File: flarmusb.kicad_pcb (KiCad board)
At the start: 2 copper layers, 22 parts, among them J1 USB_B_Micro, J2 Barrel_Jack_Switch, J3 RJ45_Shielded, U1 LM3940-3.3, U2 CH340G, U3 MAX3232, Y1 12M

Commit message: PCB traced
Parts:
- added REF**: OSHW-Logo2_9.8x8mm_SilkScreen, Symbol:OSHW-Logo2_9.8x8mm_SilkScreen, B.Cu at (110.7, 82.8)
- moved R1 36.6 mm to (128.5, 84.8), turned to 90 degrees
- moved C4 29.3 mm to (123.4, 78.2), turned to 180 degrees
- moved C7 27.6 mm to (126.5, 81.3), turned to 90 degrees
- moved C5 27.3 mm to (126.5, 84.8), turned to 90 degrees
- moved C9 26.9 mm to (135.1, 73.7), turned to 90 degrees
- moved D3 26.3 mm to (128.5, 77.7), turned to 270 degrees
- moved C6 25.5 mm to (119.9, 78.2), turned to 180 degrees
- moved D2 20.6 mm to (126.5, 77.7), turned to 270 degrees
- moved R2 19.3 mm to (128.5, 81.3), turned to 90 degrees
- moved Y1 18.5 mm to (111.1, 70.0), turned to 270 degrees
- moved C10 17.3 mm to (135.1, 68.6), turned to 270 degrees
- moved D1 14.9 mm to (111.3, 82.8), turned to 270 degrees
- moved U3 13.9 mm to (119.9, 83.3), turned to 270 degrees
- moved C8 12.6 mm to (116.3, 78.2)
- moved J3 5.85 mm to (97.2, 76.2)
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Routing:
- net 3V3: track 0.00 -> 53.4 mm, vias 0 -> 2
- net Earth: track 0.00 -> 34.9 mm, vias 0 -> 8
- net /TTL_TX: track 0.00 -> 33.9 mm, vias 0 -> 2
- net /TTL_RX: track 0.00 -> 24.4 mm
- net /12VR: track 0.00 -> 24.3 mm, vias 0 -> 2
- net /RS232_TX: track 0.00 -> 23.4 mm, vias 0 -> 1
- net /RS232_RX: track 0.00 -> 19.1 mm, vias 0 -> 1
- net Net-(C2-Pad1): track 0.00 -> 18.8 mm, vias 0 -> 1
- net /USB_D+: track 0.00 -> 18.3 mm
- net /USB_D-: track 0.00 -> 16.9 mm
- net /USB_XI: track 0.00 -> 15.8 mm, vias 0 -> 1
- net /5V: track 0.00 -> 11.5 mm
- net Net-(D2-Pad2): track 0.00 -> 9.45 mm, vias 0 -> 2
- net 12V: track 0.00 -> 8.34 mm
- net Net-(C7-Pad2): track 0.00 -> 4.63 mm
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- added copper zone on B.Cu, net Earth
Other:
- board outline added: 49.8 x 21.8 mm
- net class Default: clearance 0.2 -> 0.15; trace_width 0.25 -> 0.2; via_dia 0.8 -> 0.4; via_drill 0.4 -> 0.3
- net class HV added: clearance 0.3, trace_width 0.5, via_dia 0.6, via_drill 0.4
- net class PWR added: clearance 0.2, trace_width 0.4, via_dia 0.6, via_drill 0.4
- rule trace_clearance: 0.2 -> 0.15
- board text added: "12V"
- board text added: "FLARM"
- board text added: "FLARM-USB adapter"
- board text added: "USB"
- board text added: "by Andrey Lebedev 2019 v1.0"

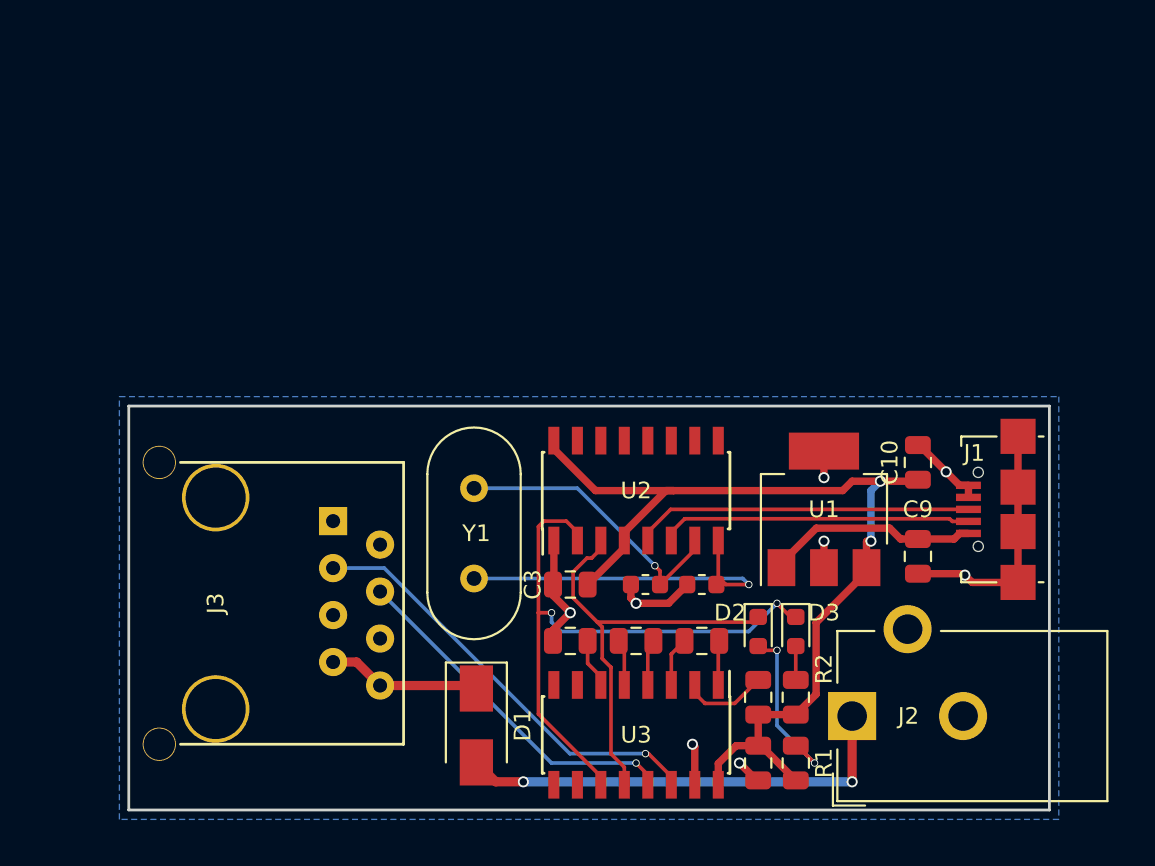
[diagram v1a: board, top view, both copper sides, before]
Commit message: New footprint for DC002 connector
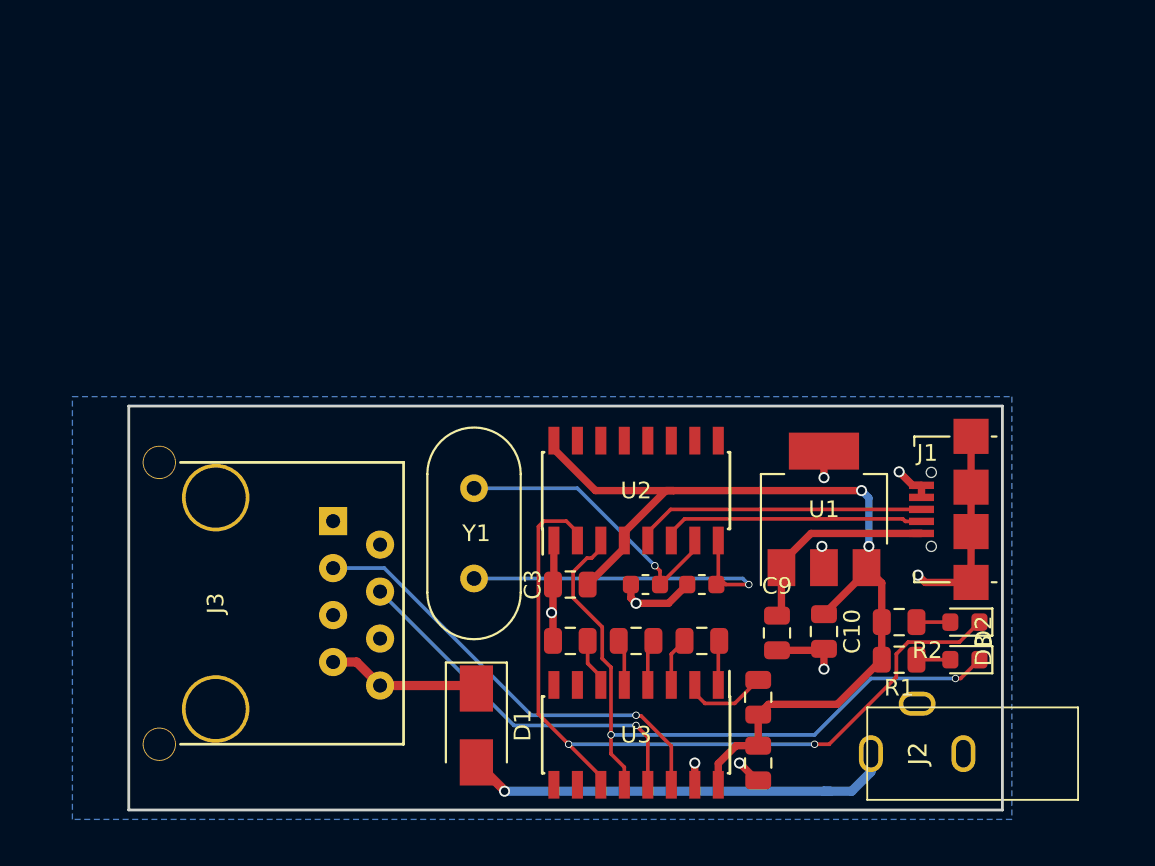
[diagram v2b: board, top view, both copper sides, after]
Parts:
- J2: footprint Connector_BarrelJack:BarrelJack_CUI_PJ-102AH_Horizontal -> flarmusb:DC002
- moved D2 11.3 mm to (137.7, 79.2), turned to 180 degrees
- moved C10 10.5 mm to (130.0, 77.7), turned to 90 degrees
- moved D3 9.16 mm to (137.7, 77.2), turned to 180 degrees
- moved C9 8.67 mm to (127.5, 77.8)
- moved R1 7.90 mm to (134.1, 79.2), turned to 0 degrees
- moved R2 6.91 mm to (134.1, 77.2), turned to 0 degrees
- moved J1 2.54 mm to (136.7, 71.1)
- moved J2 2.27 mm to (132.6, 84.3), turned to 180 degrees
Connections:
- net 12V renamed /12V
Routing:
- net /TTL_RX: track 24.4 -> 37.2 mm, vias 0 -> 2
- net /TTL_TX: track 33.9 -> 44.0 mm
- net Net-(D2-Pad2): track 9.45 -> 1.83 mm, vias 2 -> 0
- net Earth: track 34.9 -> 31.9 mm, vias 8 -> 9
- net /USB_D-: track 16.9 -> 14.3 mm
- net /USB_D+: track 18.3 -> 15.8 mm
- net 3V3: track 53.4 -> 52.2 mm
- net /RS232_RX: track 19.1 -> 20.3 mm
- net /RS232_TX: track 23.4 -> 24.4 mm
- net /12VR: vias 2 -> 1
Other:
- board size 49.8 x 21.8 mm -> 47.2 x 21.8 mm
